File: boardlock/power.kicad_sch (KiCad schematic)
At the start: 3 parts, among them U2 BQ24075RGT, U7 BQ27441DRZR-G1A, U8 TPS630701RNMR

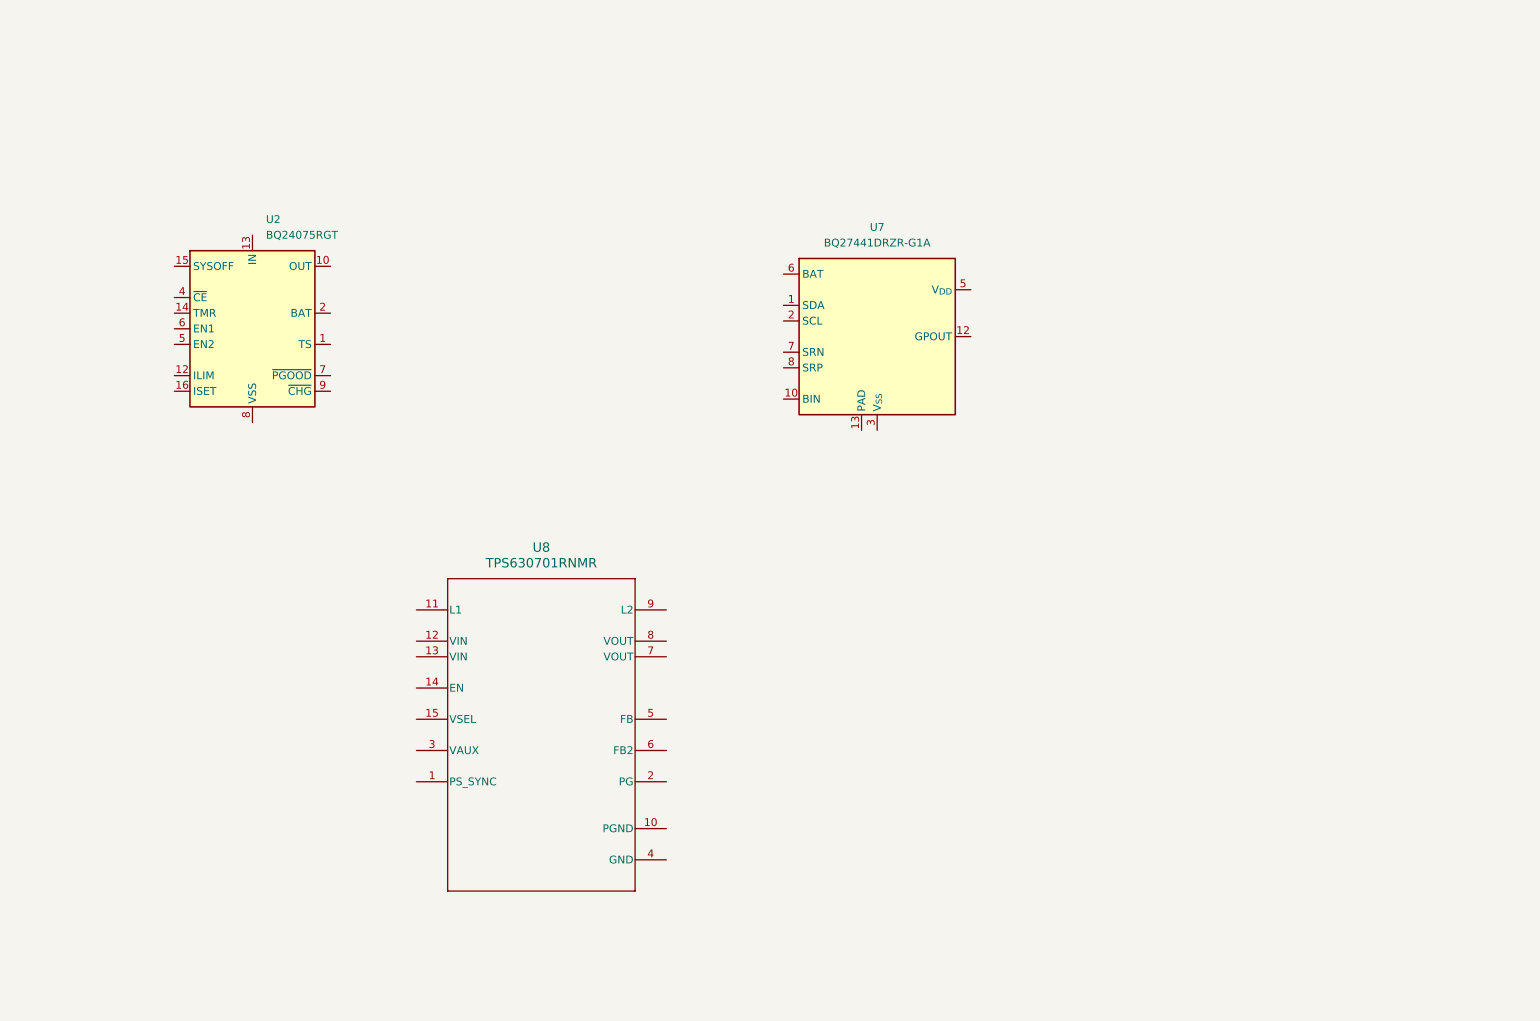
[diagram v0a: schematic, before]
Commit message: updated libraries and edited symbols
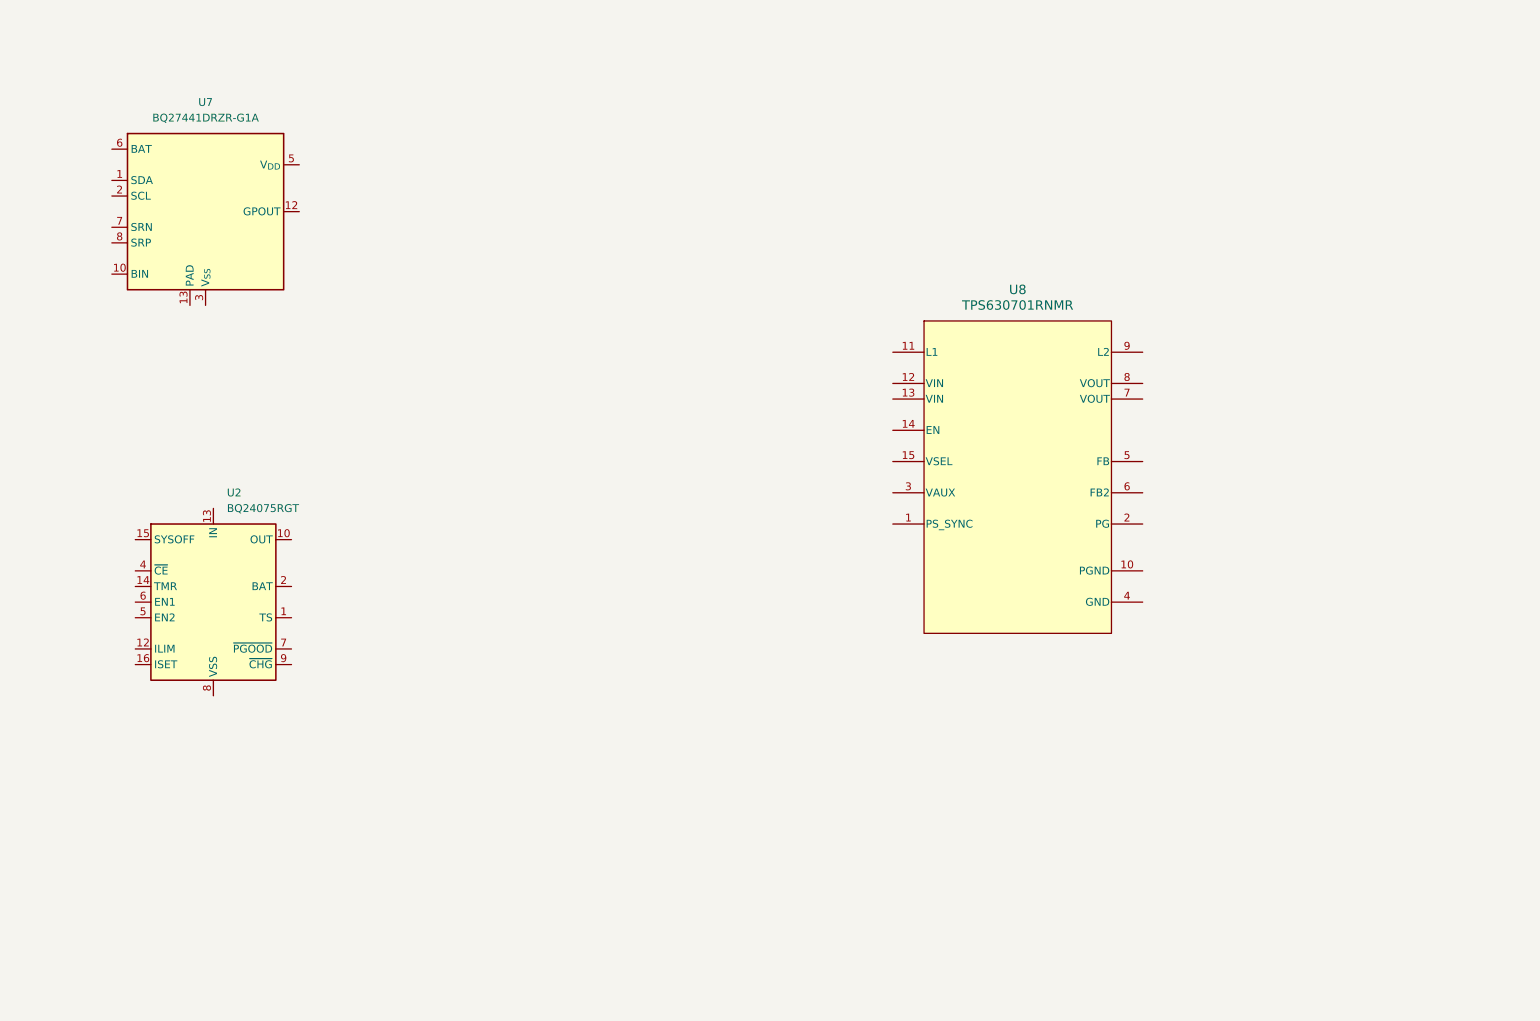
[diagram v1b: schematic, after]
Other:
- moved on the sheet: U2, U7
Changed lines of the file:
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@@
 (kicad_sch (version 20230121) (generator eeschema)
   (paper "A4")
-  (symbol (lib_id "Battery_Management:BQ27441DRZR-G1A") (at 166.37 69.85 0) (unit 1)
+  (symbol (lib_id "TPS630701RNMR:TPS630701RNMR") (at 189.23 92.71 0) (unit 1)
     (in_bom yes) (on_board yes) (dnp no) (fields_autoplaced)
-    (property "Reference" "U7" (at 166.37 52.07 0)
+    (property "Reference" "U8" (at 189.23 62.23 0)
+      (effects (font (size 1.524 1.524)))
+    )
+    (property "Value" "TPS630701RNMR" (at 189.23 64.77 0)
+      (effects (font (size 1.524 1.524)))
+    )
+    (property "Footprint" "TPS630701RNMR:TPS630701RNMR" (at 189.23 92.71 0)
+      (effects (font (size 1.27 1.27) italic) hide)
+    )
+    (property "Datasheet" "TPS630701RNMR" (at 189.23 92.71 0)
+      (effects (font (size 1.27 1.27) italic) hide)
+    )
+    (pin "1")
+    (pin "10")
+    (pin "11")
+    (pin "13")
+    (pin "14")
+    (pin "15")
+    (pin "2")
+    (pin "3")
+    (pin "4")
+    (pin "5")
+    (pin "6")
+    (pin "7")
+    (pin "8")
+    (pin "9")
+    (pin "12")
+    (instances
+      (project "boardlock"
+        (path "/e1fc29ce-837e-4062-84d8-c7e423f9eab9/5801071c-337d-449a-92e5-5afeb5febc0d"
+          (reference "U8") (unit 1)
+        )
+      )
+    )
+  )
+  (symbol (lib_id "Battery_Management:BQ27441DRZR-G1A") (at 57.15 49.53 0) (unit 1)
+    (in_bom yes) (on_board yes) (dnp no) (fields_autoplaced)
+    (property "Reference" "U7" (at 57.15 31.75 0)
       (effects (font (size 1.27 1.27)))
     )
-    (property "Value" "BQ27441DRZR-G1A" (at 166.37 54.61 0)
+    (property "Value" "BQ27441DRZR-G1A" (at 57.15 34.29 0)
       (effects (font (size 1.27 1.27)))
     )
-    (property "Footprint" "Package_SON:Texas_S-PDSO-N12" (at 172.72 83.82 0)
+    (property "Footprint" "Package_SON:Texas_S-PDSO-N12" (at 63.5 63.5 0)
       (effects (font (size 1.27 1.27)) (justify left) hide)
     )
-    (property "Datasheet" "http://www.ti.com/lit/ds/symlink/bq27441-g1.pdf" (at 171.45 64.77 0)
+    (property "Datasheet" "http://www.ti.com/lit/ds/symlink/bq27441-g1.pdf" (at 62.23 44.45 0)
       (effects (font (size 1.27 1.27)) hide)
     )
@@
     )
   )
-  (symbol (lib_id "Battery_Management:BQ24075RGT") (at 64.77 68.58 0) (unit 1)
+  (symbol (lib_id "Battery_Management:BQ24075RGT") (at 58.42 113.03 0) (unit 1)
     (in_bom yes) (on_board yes) (dnp no) (fields_autoplaced)
-    (property "Reference" "U2" (at 66.9641 50.8 0)
+    (property "Reference" "U2" (at 60.6141 95.25 0)
       (effects (font (size 1.27 1.27)) (justify left))
     )
-    (property "Value" "BQ24075RGT" (at 66.9641 53.34 0)
+    (property "Value" "BQ24075RGT" (at 60.6141 97.79 0)
       (effects (font (size 1.27 1.27)) (justify left))
     )
-    (property "Footprint" "Package_DFN_QFN:VQFN-16-1EP_3x3mm_P0.5mm_EP1.6x1.6mm" (at 72.39 82.55 0)
+    (property "Footprint" "Package_DFN_QFN:VQFN-16-1EP_3x3mm_P0.5mm_EP1.6x1.6mm" (at 66.04 127 0)
       (effects (font (size 1.27 1.27)) (justify left) hide)
     )
-    (property "Datasheet" "http://www.ti.com/lit/ds/symlink/bq24075.pdf" (at 72.39 63.5 0)
+    (property "Datasheet" "http://www.ti.com/lit/ds/symlink/bq24075.pdf" (at 66.04 107.95 0)
       (effects (font (size 1.27 1.27)) hide)
     )
@@
         )
       )
-    )
-  )
-  (symbol (lib_id "TPS630701RNMR:TPS630701RNMR") (at 111.76 134.62 0) (unit 1)
-    (in_bom yes) (on_board yes) (dnp no) (fields_autoplaced)
-    (property "Reference" "U8" (at 111.76 104.14 0)
-      (effects (font (size 1.524 1.524)))
-    )
-    (property "Value" "TPS630701RNMR" (at 111.76 106.68 0)
-      (effects (font (size 1.524 1.524)))
-    )
-    (property "Footprint" "TPS630701RNMR:TPS630701RNMR" (at 111.76 134.62 0)
-      (effects (font (size 1.27 1.27) italic) hide)
-    )
-    (property "Datasheet" "TPS630701RNMR" (at 111.76 134.62 0)
-      (effects (font (size 1.27 1.27) italic) hide)
-    )
-    (pin "1")
-    (pin "10")
-    (pin "11")
-    (pin "12")
-    (pin "13")
-    (pin "14")
-    (pin "15")
-    (pin "2")
-    (pin "3")
-    (pin "4")
-    (pin "5")
-    (pin "6")
-    (pin "7")
-    (pin "8")
-    (pin "9")
-    (instances
-      (project "boardlock"
-        (path "/e1fc29ce-837e-4062-84d8-c7e423f9eab9/5801071c-337d-449a-92e5-5afeb5febc0d"
-          (reference "U8") (unit 1)
-        )
-      )

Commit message: added buck boost topology
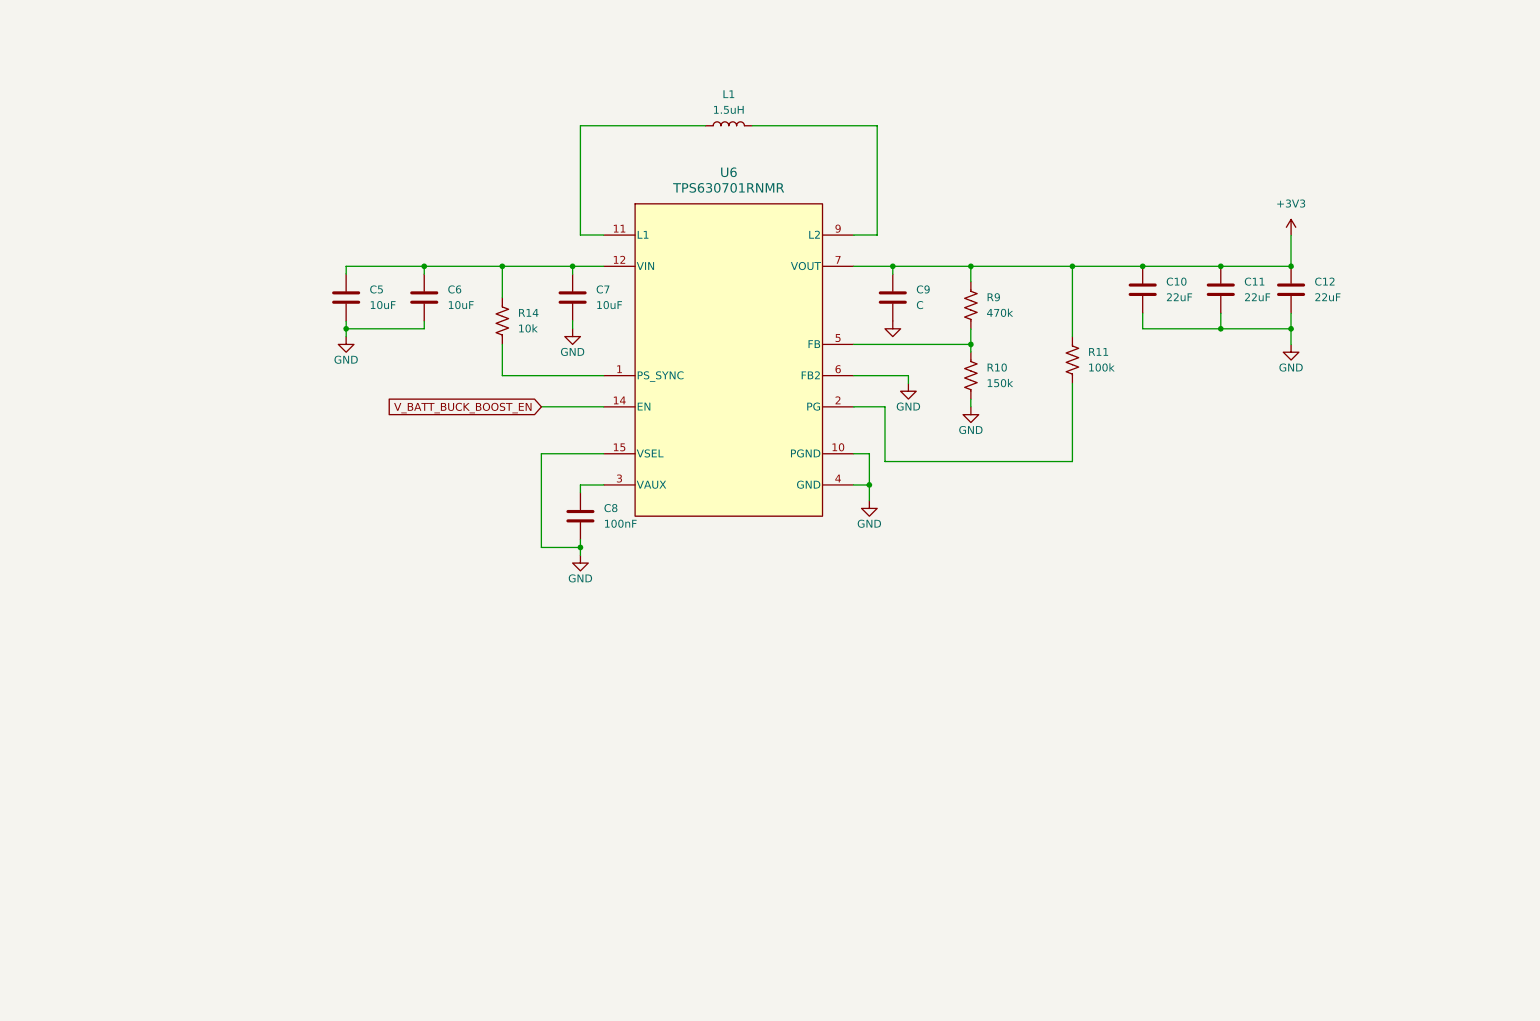
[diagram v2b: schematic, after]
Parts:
- removed U2: BQ24075RGT, Package_DFN_QFN:VQFN-16-1EP_3x3mm_P0.5mm_EP1.6x1.6mm, symbol Battery_Management:BQ24075RGT
- removed U7: BQ27441DRZR-G1A, Package_SON:Texas_S-PDSO-N12, symbol Battery_Management:BQ27441DRZR-G1A
- added C10, C11, C12: 22uF, symbol Device:C
- added C5, C6, C7: 10uF, symbol Device:C
- added C8: 100nF, symbol Device:C
- added C9: C, symbol Device:C
- added L1: 1.5uH, symbol Device:L
- added R10: 150k, symbol Device:R_US
- added R11: 100k, symbol Device:R_US
- added R14: 10k, symbol Device:R_US
- added R9: 470k, symbol Device:R_US
- renumbered U8 to U6
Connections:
- net at U6.1 (PS_SYNC): now also R14.2
- net GND: now reaches U6.10 (PGND)
- net GND: now also U6.15 (VSEL), U6.4 (GND), U6.6 (FB2), C10.2, C11.2, C12.2, C5.2, C6.2, C7.2, C8.2, C9.2, R10.2
- net at U6.11 (L1): now also L1.1
- net VIN: now reaches U6.12 (VIN)
- net VIN: now also U6.13 (VIN), C5.1, C6.1, C7.1, R14.1
- net V_BATT_BUCK_BOOST_EN: now reaches U6.14 (EN)
- net at U6.2 (PG): now also R11.2
- net at U6.3 (VAUX): now also C8.1
- net at U6.5 (FB): now also R10.1, R9.2
- net +3V3: now reaches U6.7 (VOUT)
- net +3V3: now also U6.8 (VOUT), C10.1, C11.1, C12.1, C9.1, R11.1, R9.1
- net at U6.9 (L2): now also L1.2

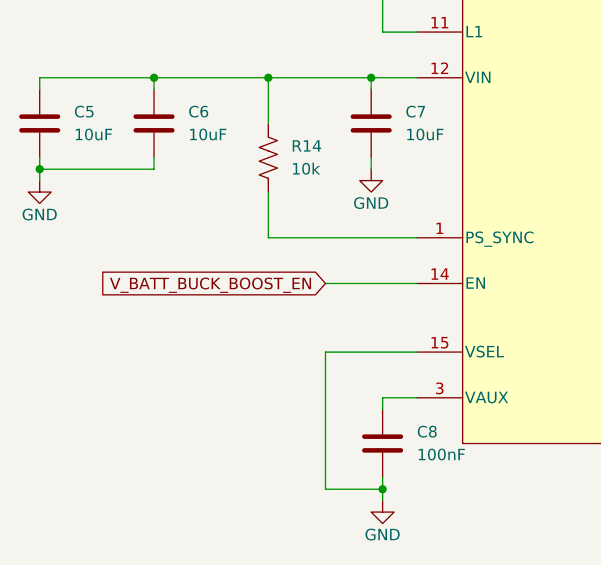
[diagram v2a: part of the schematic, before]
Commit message: edited battery management
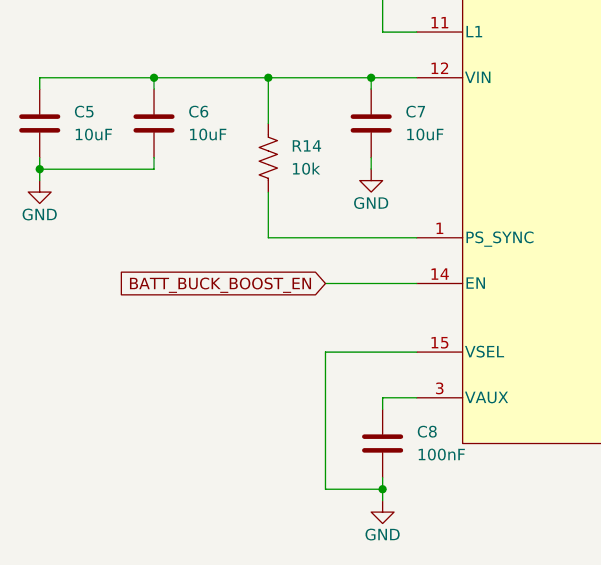
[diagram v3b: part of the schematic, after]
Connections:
- net V_BATT_BUCK_BOOST_EN renamed BATT_BUCK_BOOST_EN
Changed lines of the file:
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@@
     (stroke (width 0) (type default))
   )
-  (global_label "V_BATT_BUCK_BOOST_EN" (shape input) (at 111.76 81.28 180) (fields_autoplaced)
+  (global_label "BATT_BUCK_BOOST_EN" (shape input) (at 111.76 81.28 180) (fields_autoplaced)
     (effects (font (size 1.27 1.27)) (justify right))
-    (property "Intersheetrefs" "${INTERSHEET_REFS}" (at 85.7939 81.28 0)
+    (property "Intersheetrefs" "${INTERSHEET_REFS}" (at 87.8501 81.28 0)
       (effects (font (size 1.27 1.27)) (justify right) hide)
     )

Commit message: Zecong edits
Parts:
- added R? (x2): 330k, symbol Device:R_US
- added R?: 560k, symbol Device:R_US
- added U?: MCP1661, Package_TO_SOT_SMD:SOT-23-5, symbol Driver_LED:MCP1662-xOT
- C9: value C -> 10uF
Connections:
- net BATT_BUCK_BOOST_EN: now also R?.1, R?.1, R?.2
- net GND: now also R?.2, R?.2
- new net +BATT: R?.1
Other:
- note added: "For 3V3 output use R1 = 470k, R2 = 150k"
- note added: "Min EN pin input current = 2uA"
- note added: "Monitors battery voltage for buck-boost converter. Voltage divider calculation done at V_BATT = 3V. Buck-boost converter EN shuts off at 0.7V. V_BATT_BUCK_BOOST_EN = 0.683 @ VBATT = 3V"
- note added: "NOTE: Repurposed MCP1662 Symbol"
- note added: "Resistors: Metal Film 1%"
- note added: "TI reccomends 0603 10uF to put near Vin and Vout pins"
- moved on the sheet: C10, C11, C12, C5, C6, C7, C8, C9, L1, R10, R11, R14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

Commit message: More zecong edits
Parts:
- removed U?: MCP1661, Package_TO_SOT_SMD:SOT-23-5, symbol Driver_LED:MCP1662-xOT
- C7, C9: footprint (none) -> Resistor_SMD:R_0603_1608Metric_Pad0.98x0.95mm_HandSolder
- C8: footprint (none) -> Resistor_SMD:R_0402_1005Metric_Pad0.72x0.64mm_HandSolder
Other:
- note added: "3V3 Buck-Boost"
- note removed: "NOTE: Repurposed MCP1662 Symbol"
- company: (none) -> Schetmatic
- title: (none) -> BoardLock Schematic
- moved on the sheet: C10, C11, C12, C5, C6, C7, C8, C9, L1, R10, R11, R14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

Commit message: saving
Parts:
- added C? (x2): 10uF, symbol Device:C
- added D?: PMEG2005EH, Diode_SMD:D_SOD-123F, symbol Diode:PMEG2005EH
- added L?: 4.7uH, symbol Device:L
- added R?: 1.05M, symbol Device:R_US
- added R?: 120k, symbol Device:R_US
- added U?: MCP1661, Package_TO_SOT_SMD:SOT-23-5, symbol Driver_LED:MCP1662-xOT
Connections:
- net +3V3: now also C?.1, L?.1, U?.5 (V_{IN})
- net GND: now also C?.2, C?.2, R?.2, U?.2 (GND)
- new net: R?.1, R?.2, U?.3 (V_{FB})
- new net: D?.2 (A), L?.2, U?.1 (SW)
- new net +12V: C?.1, D?.1 (K), R?.1
- new net M_BOOST_EN: U?.4 (EN)
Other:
- note added: "12V Boost Converter"
- note added: "NOTE: Repurposed MCP1662 Symbol"
- note added: "V_FB = 1.227V"
- moved on the sheet: C10, C11, C12, C5, C6, C7, C8, C9, L1, R10, R11, R14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
